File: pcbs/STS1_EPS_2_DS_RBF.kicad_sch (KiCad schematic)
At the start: 33 parts, among them Q1 2N7002, Q10 2N7002, Q11 2N7002, Q14 2N7002, Q15 2N7002, Q18 2N7002, Q19 2N7002, Q20 2N7002, Q7 2N7002

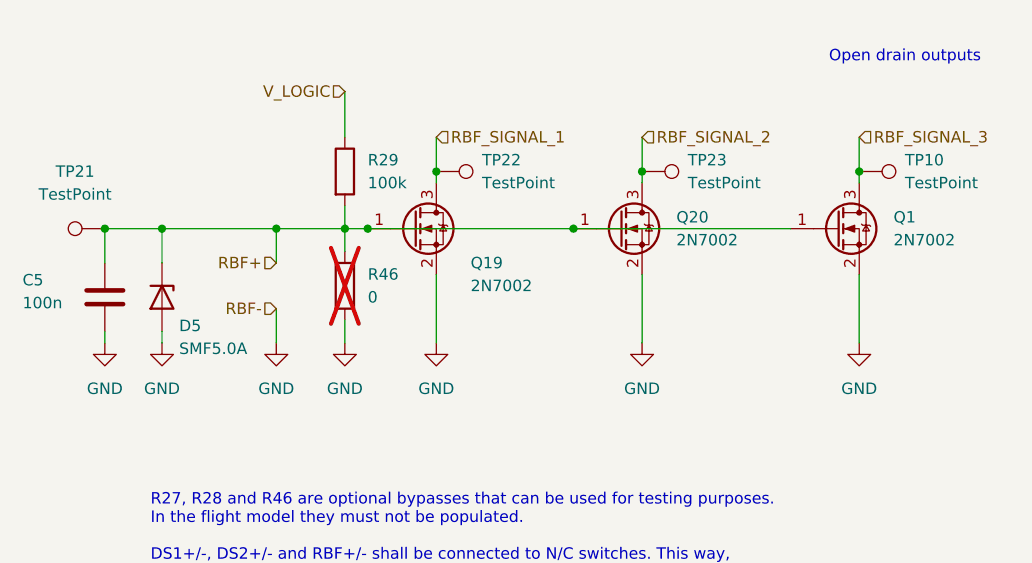
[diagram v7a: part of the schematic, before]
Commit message: Fixed inhibit logic.
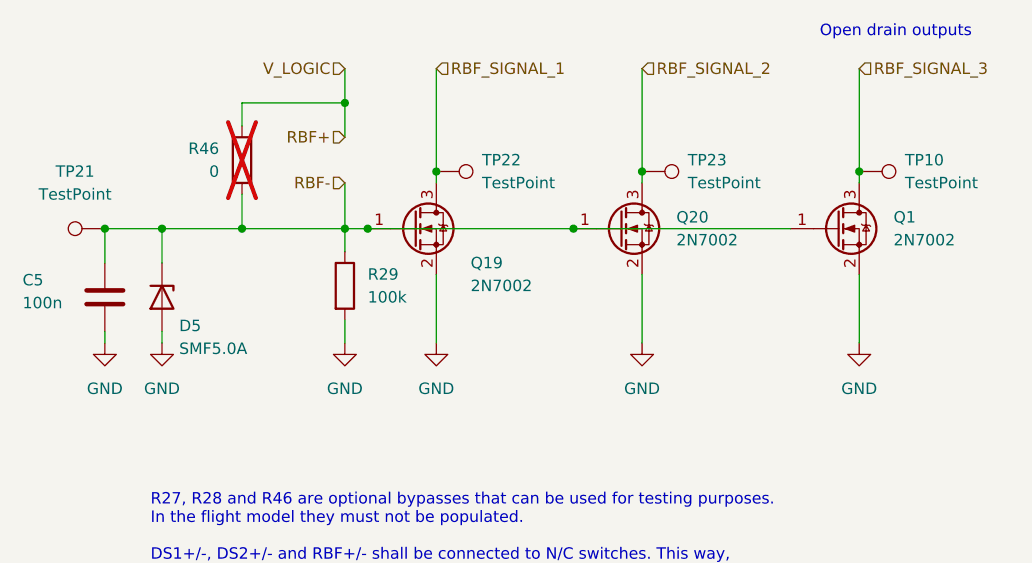
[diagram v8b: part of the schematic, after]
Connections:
- net GND: now also R29.2; no longer R46.2
- net RBF+: now also R25.1, R26.1, R46.2; no longer C5.1, D5.1 (K), Q1.1 (G), Q19.1 (G), Q20.1 (G), R29.2, R46.1, TP21.1
- removed net V_LOGIC: R25.1, R26.1, R29.1
- new net RBF-: C5.1, D5.1 (K), Q1.1 (G), Q19.1 (G), Q20.1 (G), R29.1, R46.1, TP21.1
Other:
- moved on the sheet: R29, R46
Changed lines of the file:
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@@
 	)
 	(junction
-		(at 140.97 40.64)
+		(at 137.16 40.64)
 		(diameter 0)
 		(color 0 0 0 0)
@@
 	)
 	(junction
+		(at 148.59 26.67)
+		(diameter 0)
+		(color 0 0 0 0)
+	)
+	(junction
 		(at 29.21 81.28)
 		(diameter 0)
@@
 	(wire
 		(pts
-			(xy 148.59 25.4) (xy 148.59 30.48)
+			(xy 148.59 22.86) (xy 148.59 26.67)
 		)
 		(stroke
@@
 	(wire
 		(pts
+			(xy 148.59 26.67) (xy 148.59 30.48)
+		)
+		(stroke
+			(width 0)
+			(type default)
+		)
+	)
+	(wire
+		(pts
 			(xy 20.32 90.17) (xy 20.32 91.44)
 		)
@@
 	(wire
 		(pts
+			(xy 137.16 40.64) (xy 148.59 40.64)
+		)
+		(stroke
+			(width 0)
+			(type default)
+		)
+	)
+	(wire
+		(pts
 			(xy 64.77 33.02) (xy 64.77 34.29)
 		)
@@
 	(wire
 		(pts
-			(xy 148.59 38.1) (xy 148.59 40.64)
+			(xy 148.59 35.56) (xy 148.59 40.64)
 		)
 		(stroke
@@
 	(wire
 		(pts
-			(xy 140.97 40.64) (xy 148.59 40.64)
+			(xy 128.27 40.64) (xy 137.16 40.64)
 		)
 		(stroke
@@
 	(wire
 		(pts
-			(xy 140.97 40.64) (xy 140.97 44.45)
+			(xy 148.59 26.67) (xy 137.16 26.67)
 		)
 		(stroke
@@
 	(wire
 		(pts
-			(xy 205.74 30.48) (xy 205.74 34.29)
+			(xy 205.74 22.86) (xy 205.74 34.29)
 		)
 		(stroke
@@
 	(wire
 		(pts
+			(xy 137.16 26.67) (xy 137.16 29.21)
+		)
+		(stroke
+			(width 0)
+			(type default)
+		)
+	)
+	(wire
+		(pts
 			(xy 35.56 88.9) (xy 35.56 91.44)
 		)
@@
 	(wire
 		(pts
-			(xy 158.75 30.48) (xy 158.75 34.29)
+			(xy 158.75 22.86) (xy 158.75 34.29)
 		)
 		(stroke
@@
 	(wire
 		(pts
-			(xy 140.97 49.53) (xy 140.97 53.34)
-		)
-		(stroke
-			(width 0)
-			(type default)
-		)
-	)
-	(wire
-		(pts
 			(xy 64.77 29.21) (xy 64.77 33.02)
 		)
@@
 	(wire
 		(pts
-			(xy 181.61 30.48) (xy 181.61 34.29)
+			(xy 181.61 22.86) (xy 181.61 34.29)
 		)
 		(stroke
@@
 	(wire
 		(pts
-			(xy 128.27 40.64) (xy 140.97 40.64)
+			(xy 121.92 40.64) (xy 121.92 44.45)
 		)
 		(stroke
@@
 	(wire
 		(pts
-			(xy 121.92 40.64) (xy 121.92 44.45)
+			(xy 83.82 83.82) (xy 83.82 91.44)
 		)
 		(stroke
@@
 	(wire
 		(pts
-			(xy 83.82 83.82) (xy 83.82 91.44)
+			(xy 35.56 39.37) (xy 38.1 39.37)
 		)
 		(stroke
@@
 	(wire
 		(pts
-			(xy 35.56 39.37) (xy 38.1 39.37)
+			(xy 45.72 29.21) (xy 45.72 33.02)
 		)
 		(stroke
@@
 	(wire
 		(pts
-			(xy 45.72 29.21) (xy 45.72 33.02)
+			(xy 20.32 78.74) (xy 20.32 82.55)
 		)
 		(stroke
@@
 	(wire
 		(pts
-			(xy 20.32 78.74) (xy 20.32 82.55)
+			(xy 173.99 40.64) (xy 198.12 40.64)
 		)
 		(stroke
@@
 	(wire
 		(pts
-			(xy 173.99 40.64) (xy 198.12 40.64)
+			(xy 137.16 36.83) (xy 137.16 40.64)
 		)
 		(stroke
@@
 	(text "Open drain outputs"
 		(exclude_from_sim no)
-		(at 210.82 21.59 0)
+		(at 209.804 18.796 0)
 		(effects
 			(font
@@
 	(hierarchical_label "RBF_SIGNAL_3"
 		(shape input)
-		(at 205.74 30.48 0)
+		(at 205.74 22.86 0)
 		(fields_autoplaced yes)
 		(effects
@@
 	(hierarchical_label "RBF+"
 		(shape input)
-		(at 140.97 44.45 180)
+		(at 148.59 30.48 180)
 		(fields_autoplaced yes)
 		(effects
@@
 	(hierarchical_label "RBF-"
 		(shape input)
-		(at 140.97 49.53 180)
+		(at 148.59 35.56 180)
 		(fields_autoplaced yes)
 		(effects
@@
 	(hierarchical_label "RBF_SIGNAL_2"
 		(shape input)
-		(at 181.61 30.48 0)
+		(at 181.61 22.86 0)
 		(fields_autoplaced yes)
 		(effects
@@
 	(hierarchical_label "V_LOGIC"
 		(shape input)
-		(at 148.59 25.4 180)
+		(at 148.59 22.86 180)
 		(fields_autoplaced yes)
 		(effects
@@
 	(hierarchical_label "RBF_SIGNAL_1"
 		(shape input)
-		(at 158.75 30.48 0)
+		(at 158.75 22.86 0)
 		(fields_autoplaced yes)
 		(effects
@@
 	(symbol
 		(lib_id "power:GND")
-		(at 140.97 53.34 0)
-		(unit 1)
-		(exclude_from_sim no)
-		(in_bom yes)
-		(on_board yes)
-		(dnp no)
-		(fields_autoplaced yes)
-		(property "Reference" "#PWR061"
-			(at 140.97 59.69 0)
-			(effects
-				(font
-					(size 1.27 1.27)
-				)
-				(hide yes)
-			)
-		)
-		(property "Value" "GND"
-			(at 140.97 58.42 0)
-			(effects
-				(font
-					(size 1.27 1.27)
-				)
-			)
-		)
-		(property "Footprint" ""
-			(at 140.97 53.34 0)
-			(effects
-				(font
-					(size 1.27 1.27)
-				)
-				(hide yes)
-			)
-		)
-		(property "Datasheet" ""
-			(at 140.97 53.34 0)
-			(effects
-				(font
-					(size 1.27 1.27)
-				)
-				(hide yes)
-			)
-		)
-		(property "Description" "Power symbol creates a global label with name \"GND\" , ground"
-			(at 140.97 53.34 0)
-			(effects
-				(font
-					(size 1.27 1.27)
-				)
-				(hide yes)
-			)
-		)
-		(pin "1"
-		)
-		(instances
-			(project "STS1_EPS_2"
-				(path "/38c03ff7-ea47-4d00-b37d-ddcaa7d87722/782ccd28-d43b-446c-892c-2705ffe9f1f3"
-					(reference "#PWR061")
-					(unit 1)
-				)
-			)
-		)
-	)
-	(symbol
-		(lib_id "power:GND")
 		(at 121.92 53.34 0)
 		(unit 1)
@@
 	(symbol
 		(lib_id "Device:R")
-		(at 148.59 46.99 0)
+		(at 137.16 33.02 0)
+		(mirror x)
 		(unit 1)
 		(exclude_from_sim no)
@@
 		(on_board yes)
 		(dnp yes)
-		(fields_autoplaced yes)
 		(property "Reference" "R46"
-			(at 151.13 45.7199 0)
+			(at 134.62 31.7499 0)
 			(effects
 				(font
 					(size 1.27 1.27)
 				)
-				(justify left)
+				(justify right)
 			)
 		)
 		(property "Value" "0"
-			(at 151.13 48.2599 0)
+			(at 134.62 34.2899 0)
 			(effects
 				(font
 					(size 1.27 1.27)
 				)
-				(justify left)
+				(justify right)
 			)
 		)
 		(property "Footprint" "Resistor_SMD:R_0805_2012Metric"
-			(at 146.812 46.99 90)
+			(at 135.382 33.02 90)
 			(effects
 				(font
@@
 		)
 		(property "Datasheet" "~"
-			(at 148.59 46.99 0)
+			(at 137.16 33.02 0)
 			(effects
 				(font
@@
 		)
 		(property "Description" ""
-			(at 148.59 46.99 0)
+			(at 137.16 33.02 0)
 			(effects
 				(font
@@
 	(symbol
 		(lib_id "Device:R")
-		(at 148.59 34.29 0)
+		(at 148.59 46.99 0)
 		(unit 1)
 		(exclude_from_sim no)
@@
 		(fields_autoplaced yes)
 		(property "Reference" "R29"
-			(at 151.13 33.0199 0)
+			(at 151.13 45.7199 0)
 			(effects
 				(font
@@
 		)
 		(property "Value" "100k"
-			(at 151.13 35.5599 0)
+			(at 151.13 48.2599 0)
 			(effects
 				(font
@@
 		)
 		(property "Footprint" "Resistor_SMD:R_0805_2012Metric"
-			(at 146.812 34.29 90)
+			(at 146.812 46.99 90)
 			(effects
 				(font
@@
 		)
 		(property "Datasheet" "~"
-			(at 148.59 34.29 0)
+			(at 148.59 46.99 0)
 			(effects
 				(font
@@
 		)
 		(property "Description" ""
-			(at 148.59 34.29 0)
+			(at 148.59 46.99 0)
 			(effects
 				(font
